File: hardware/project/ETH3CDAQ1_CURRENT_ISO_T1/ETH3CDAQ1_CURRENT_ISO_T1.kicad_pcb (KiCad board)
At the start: 4 copper layers, 80 x 30 mm, 51 parts, among them J1 PC 5/2-G-7.62, J2 Conn_02x10_Odd_Even, U1 DG419xY, U10 74LVC1GU04DRL, U11 TXB0104PW, U2 DG211, U3 T60404-N4646-X400, U4 OPA140, U5 LT3032-15, U6 24LC08B-E/MS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

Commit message: PCB design
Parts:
- C8: moved to F.Cu
- FB2: moved to B.Cu
- moved FB2 12.3 mm to (138.0, 80.9), turned to 180 degrees
- moved C8 7.75 mm to (146.7, 80.9), turned to 0 degrees
- moved RV1 1.77 mm to (80.8, 67.0)
- moved C5 0.80 mm to (139.7, 75.7)
- moved C1 0.52 mm to (138.9, 74.5)
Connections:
- J2 pad 7: /ANALOG_OUT -> GND
- J2 pad 8: /ANALOG_OUT -> GND
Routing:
- net /ANALOG_OUT: track 0.00 -> 36.6 mm, vias 0 -> 2
- net -15V: track 9.09 -> 32.1 mm, vias 4 -> 8
- net /A1: track 9.62 -> 27.6 mm
- net /A0: track 4.45 -> 21.6 mm
- net +15V: track 8.69 -> 24.7 mm, vias 4 -> 7
- net Net-(U2-Pad11): track 21.5 -> 31.5 mm
- net /I2C_SDA: track 17.8 -> 26.7 mm, vias 2 -> 1
- net +5V: track 9.91 -> 16.8 mm
- net GND: track 4.48 -> 11.3 mm, vias 5 -> 12
- net +3V3: track 7.26 -> 12.0 mm, vias 4 -> 5
- net /I2C_SCL: track 19.4 -> 23.7 mm, vias 2 -> 1
- net Net-(R5-Pad2): track 8.97 -> 6.20 mm
- net -18V: track 2.33 -> 4.78 mm, vias 2 -> 3
- net +18V: track 1.28 -> 3.57 mm, vias 2 -> 4
- net /WP: track 12.5 -> 10.7 mm
- added copper zone on B.Cu, net +15V
- added copper zone on F.Cu, net +15V
- added copper zone on In2.Cu, net +15V
- added copper zone on B.Cu, net +18V
- added copper zone on F.Cu, net +18V
- added copper zone on In2.Cu, net +3V3
- added copper zone on In2.Cu, net +5V
- added copper zone on B.Cu, net -15V
- added copper zone on F.Cu, net -15V
- added copper zone on In2.Cu, net -15V
- added copper zone on B.Cu, net -18V
- added copper zone on F.Cu, net -18V
- added copper zone on In2.Cu, net -18V
- added copper zone on B.Cu, net Net-(J1-Pad1)
- added copper zone on F.Cu, net Net-(J1-Pad1)
- added copper zone on In1.Cu, net Net-(J1-Pad1)
- added copper zone on In2.Cu, net Net-(J1-Pad1)
- added copper zone on B.Cu, net Net-(J1-Pad2)
- added copper zone on F.Cu, net Net-(J1-Pad2)
- added copper zone on In1.Cu, net Net-(J1-Pad2)
- added copper zone on In2.Cu, net Net-(J1-Pad2)
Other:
- outline, holes or cut-outs redrawn

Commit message: PCB design done
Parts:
- moved U3 0.31 mm to (119.3, 67.3)
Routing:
- net Net-(J1-Pad1): track 0.00 -> 129.4 mm, vias 0 -> 39
- net Net-(J1-Pad2): track 0.00 -> 103.5 mm, vias 0 -> 39

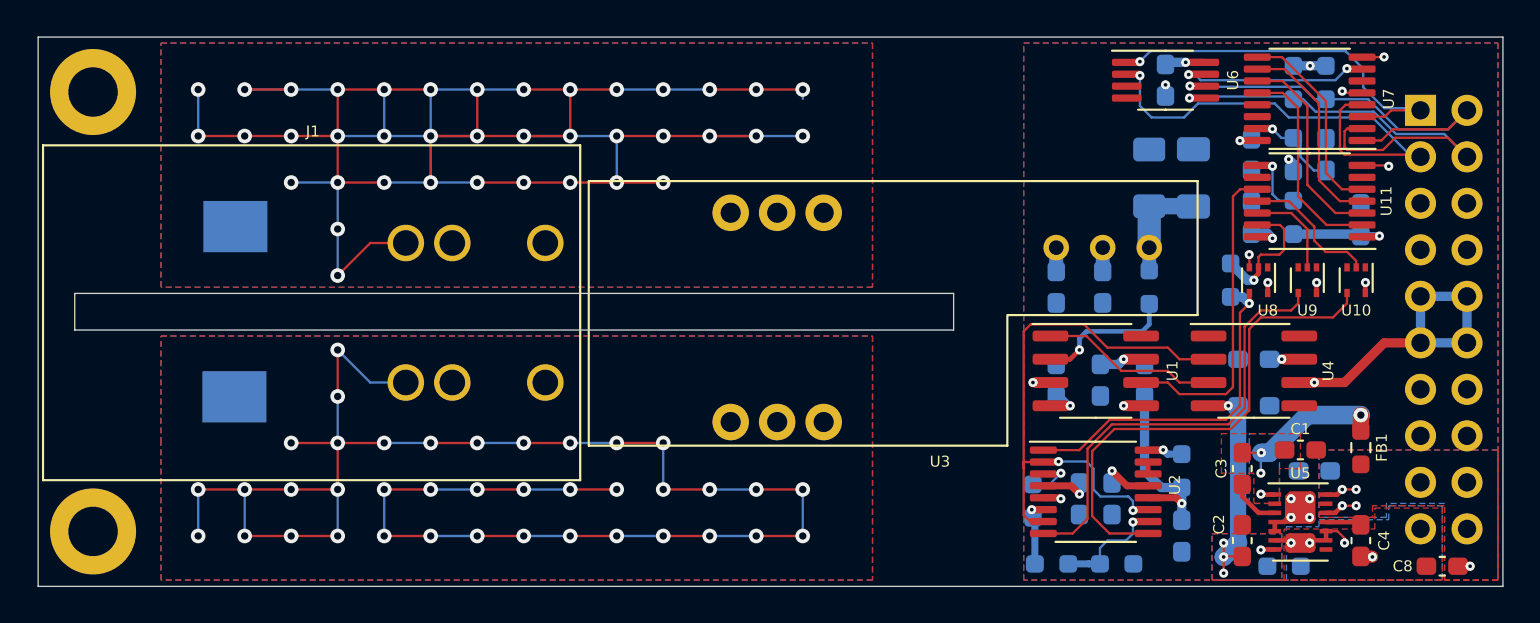
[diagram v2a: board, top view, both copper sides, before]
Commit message: Modification in PCBs. Created BOM files.
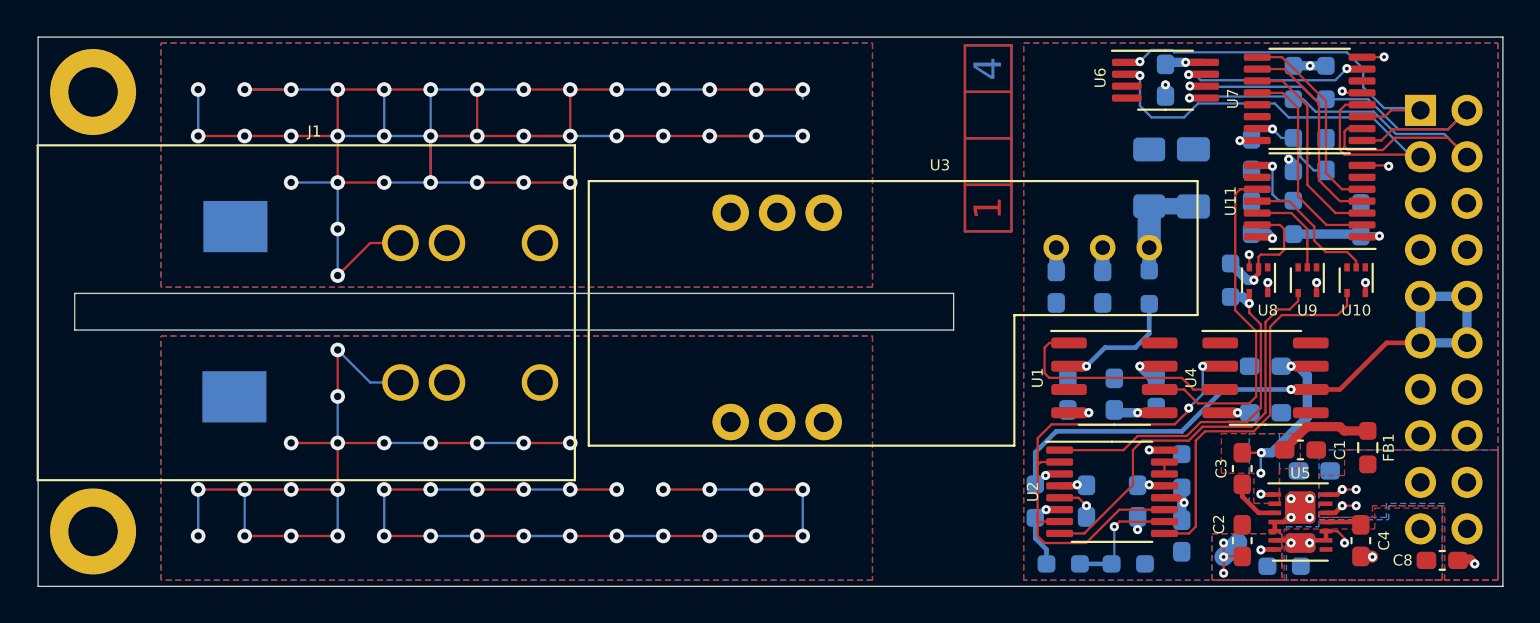
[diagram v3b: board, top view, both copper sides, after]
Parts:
- R1: value 100 -> URG3216L-101-L-T05
- moved C13 3.11 mm to (131.1, 71.4)
- moved C17 1.82 mm to (128.8, 71.5)
- moved C12 1.40 mm to (130.0, 77.3)
- moved U1 1.09 mm to (128.8, 70.6)
- moved C11 0.99 mm to (126.2, 71.5)
- moved U2 0.89 mm to (128.7, 76.8)
- moved C10 0.74 mm to (137.0, 70.0)
- moved C14 0.74 mm to (137.0, 72.5)
- moved U4 0.74 mm to (137.0, 70.6)
- moved R5 0.63 mm to (126.0, 80.8)
- moved R6 0.63 mm to (129.5, 80.8)
- moved C16 0.40 mm to (127.3, 77.3)
- moved FB1 0.38 mm to (142.6, 74.4)
- moved C8 0.32 mm to (146.7, 80.6)
- moved J1 0.29 mm to (84.7, 67.1)
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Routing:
- net (no net): track 0.00 -> 132.1 mm
- net Net-(J1-Pad2): track 103.5 -> 95.9 mm, vias 39 -> 37
- net Net-(J1-Pad1): track 129.4 -> 121.8 mm, vias 39 -> 37
- net /G100: track 27.4 -> 21.4 mm
- net Net-(U1-Pad1): track 9.69 -> 12.8 mm
- net +15V: track 24.7 -> 21.8 mm, vias 7 -> 6
- net Net-(U2-Pad11): track 31.5 -> 28.7 mm
- net -15V: track 32.1 -> 34.7 mm
- net /G10: track 24.5 -> 22.7 mm
- net /AZ: track 17.3 -> 18.6 mm
- net Net-(R2-Pad2): track 3.19 -> 4.28 mm
- net +5V: track 16.8 -> 15.8 mm
- net Net-(R3-Pad1): track 7.68 -> 6.74 mm
- net Net-(R7-Pad1): track 1.94 -> 2.71 mm
- net GND: track 11.3 -> 12.1 mm
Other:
- board text added: "1"
- board text added: "2"
- board text added: "3"
- board text added: "4"

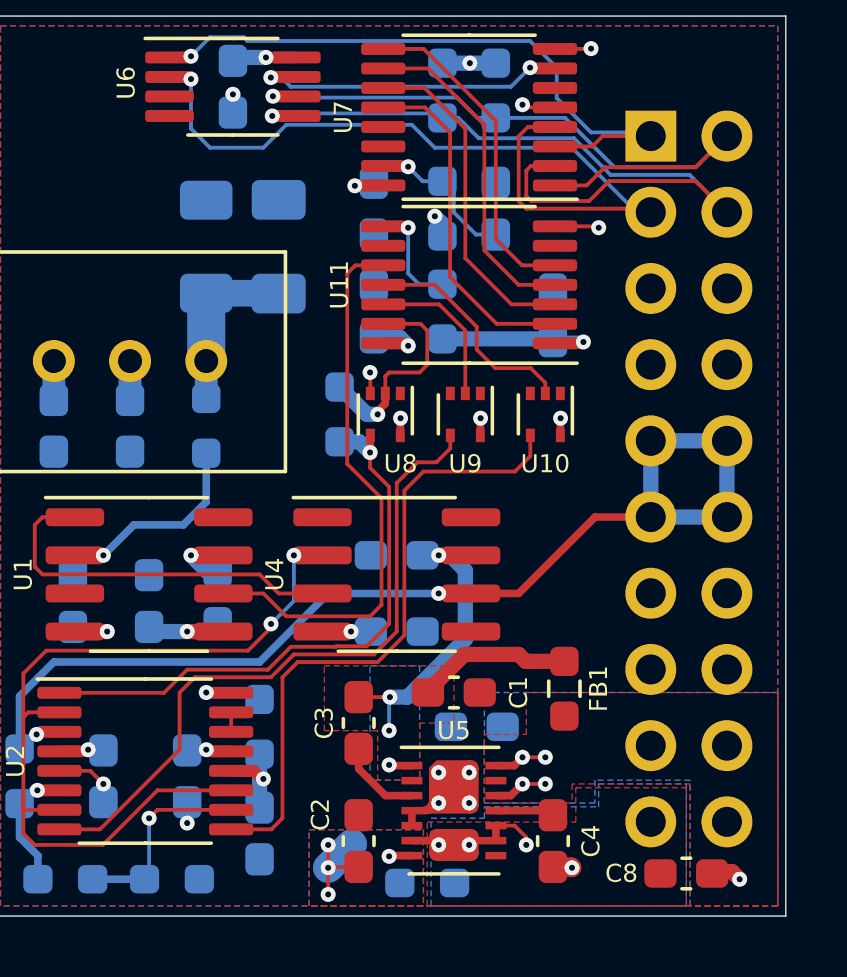
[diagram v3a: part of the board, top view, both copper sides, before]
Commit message: Modification in measurement module PCB.
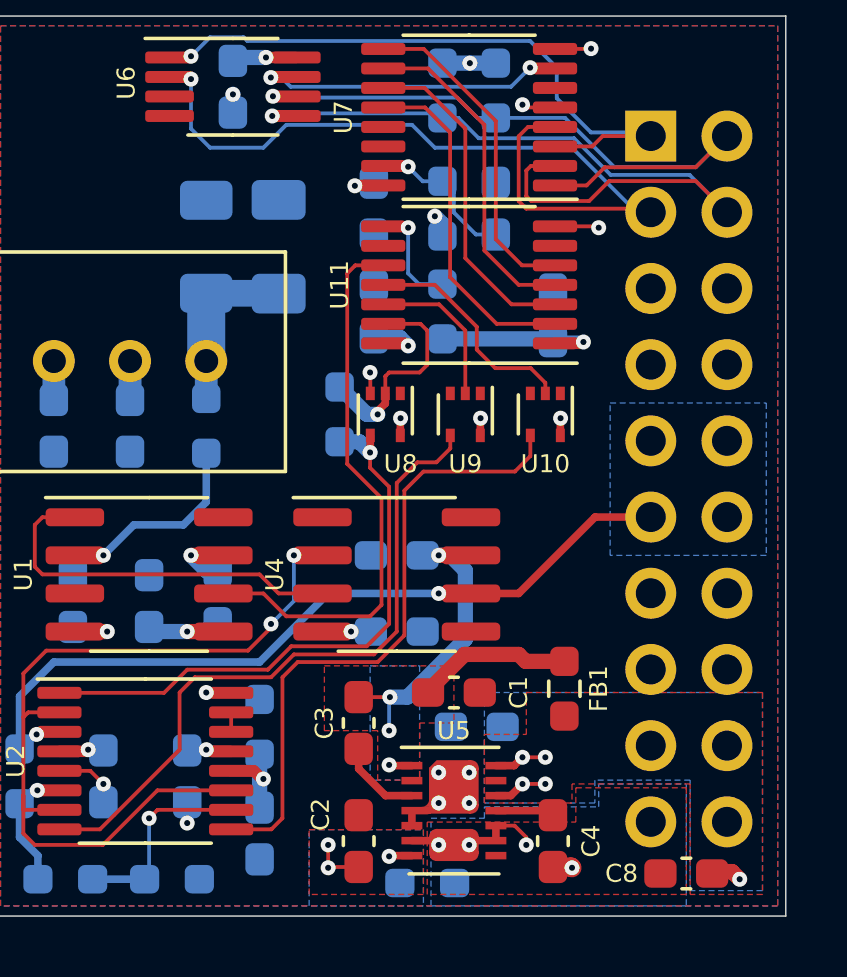
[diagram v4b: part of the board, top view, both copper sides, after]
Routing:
- net /ANALOG_OUT: track 37.0 -> 26.8 mm
- net -15V: track 34.7 -> 32.7 mm, vias 8 -> 7
- added copper zone on B.Cu, net /ANALOG_OUT

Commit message: PCB design
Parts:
- added R12: 10k, Resistor_SMD:R_0603_1608Metric_Pad0.98x0.95mm_HandSolder, B.Cu at (133.0, 65.7)
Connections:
- U1 pad 8: GND -> Net-(R12-Pad1)
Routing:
- net Net-(R12-Pad1): track 0.00 -> 3.41 mm, vias 0 -> 1

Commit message: PCB modifications
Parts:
- moved U3 0.25 mm to (119.3, 67.1)
- moved RV1 0.06 mm to (80.8, 67.1)
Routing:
- net Net-(J1-Pad1): track 121.8 -> 121.3 mm

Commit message: Changed 24LC08 to 24LC024. Added fixes to ethernetif.c to solve the problem with D Cache and RX deadlock. The fixes are also in ethernetif_fix.c, because code generator will overwrite ethernetif.c.
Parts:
- U1: value DG419xY -> DG419DY
- U6: value 24LC08B-E/MS -> 24LC024T-I/MS
